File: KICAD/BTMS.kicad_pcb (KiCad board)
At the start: 2 copper layers, 0.1 x 46.8 mm, 139 parts, among them J1 Conn_01x05_Male, J2 AUX_Charge, J3 Battery_IO, J4 Power_Out, J5 BTemp, J6 DSKY, J7 key, J8 ICSP, P1 USB_C_Plug, Q1 SSM3K341R, Q2 DMN65D8L, Q3 SSM3K341R, Q4 FDN340P, Q5 FDN340P, Q6 FDN340P, Q7 DMN65D8L, Q8 DMN65D8L, U1 ACS711xLCTR-25AB, U10 BA033CC0FP-E2, U11 AON7522E, U12 AON7522E, U13 LM62CIM3/NOPB, U14 FAN3100TSX, U15 FAN3100TSX, U16 AON7522E, U17 dsPIC30F3011-PT, U18 FT230XQ, U2 AP33771, U3 IS281-4, U4 Q294700DSGR, U5 SCF4030-12-0X, U6 AONR21321, U7 ACS711xLCTR-25AB, U8 IS281-4, U9 IRS2184

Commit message: Fixed 3.3v regulator not having correct pinout. Progressed board layout.
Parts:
- added J9: Heater, Connector_PinHeader_2.54mm:PinHeader_1x02_P2.54mm_Vertical, F.Cu at (183.5, 143.4)
- J1: value Conn_01x05_Male -> Batt_Ballance
- J7: value key -> PWR_SW
- moved J7 189.1 mm to (205.0, 143.3), turned to -90 degrees
- moved C24 178.3 mm to (112.9, 132.3), turned to -90 degrees
- moved D18 173.8 mm to (115.0, 127.6), turned to 90 degrees
- moved C16 173.2 mm to (112.8, 136.0), turned to 90 degrees
- moved C32 172.8 mm to (115.3, 96.8)
- moved C35 168.2 mm to (118.9, 97.0)
- moved C20 166.2 mm to (115.4, 123.9)
- moved C12 165.5 mm to (120.4, 136.8), turned to 90 degrees
- moved Q4 161.4 mm to (190.3, 104.4), turned to 90 degrees
- moved U7 161.2 mm to (116.7, 134.6), turned to -90 degrees
- moved C41 160.7 mm to (189.0, 113.3), turned to -90 degrees
- moved L1 160.1 mm to (120.1, 110.2), turned to 90 degrees
- moved D24 159.4 mm to (187.2, 113.3), turned to 90 degrees
- moved R10 158.4 mm to (113.4, 119.6), turned to 90 degrees
- moved C42 157.0 mm to (190.0, 116.6), turned to -90 degrees
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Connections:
- Q3 pad 3: unconnected-(Q3-Pad3) -> Net-(Q3-Pad3)
- U10 pad 1: GND -> Net-(C13-Pad1)
- U10 pad 2: +5C -> GND
- U10 pad 3: Net-(C13-Pad1) -> +5C
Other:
- board size 0.1 x 46.8 mm -> 99.8 x 59.4 mm

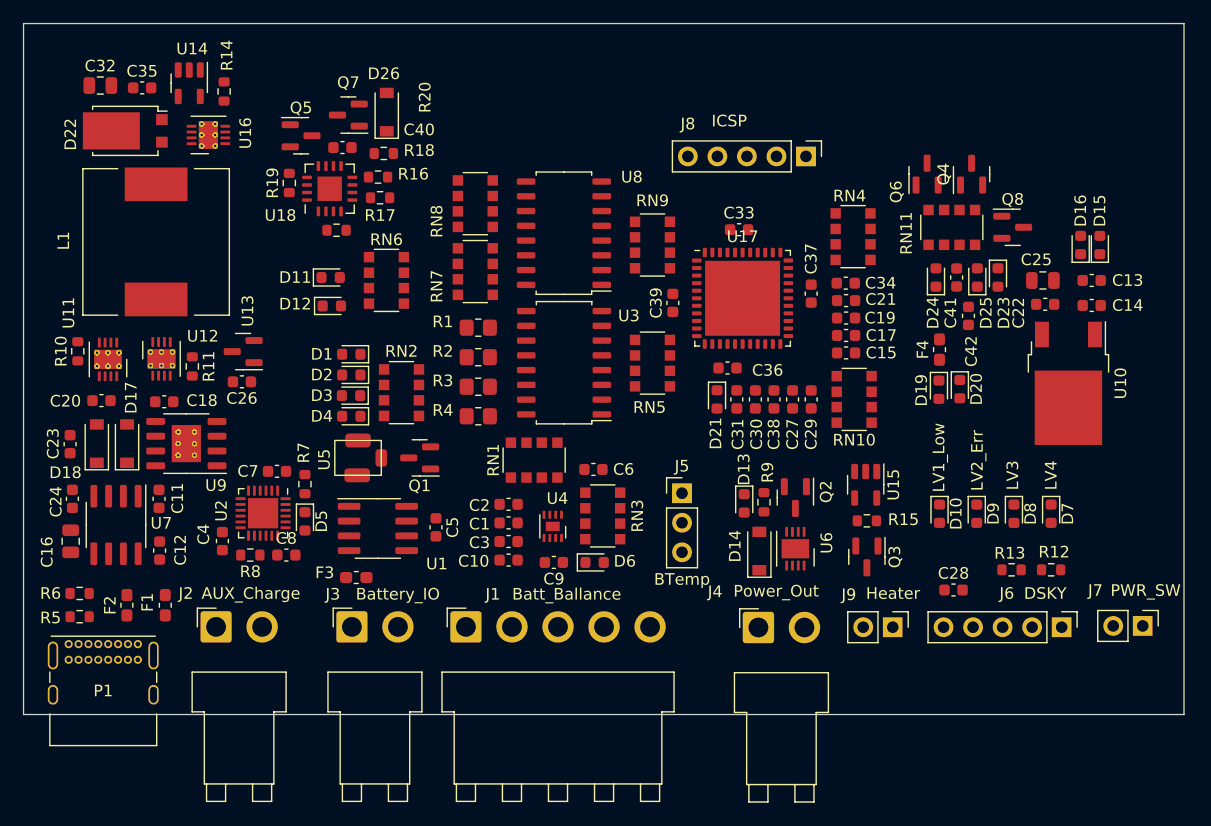
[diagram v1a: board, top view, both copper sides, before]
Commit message: Shrunk silkscreen text to compact parts more.
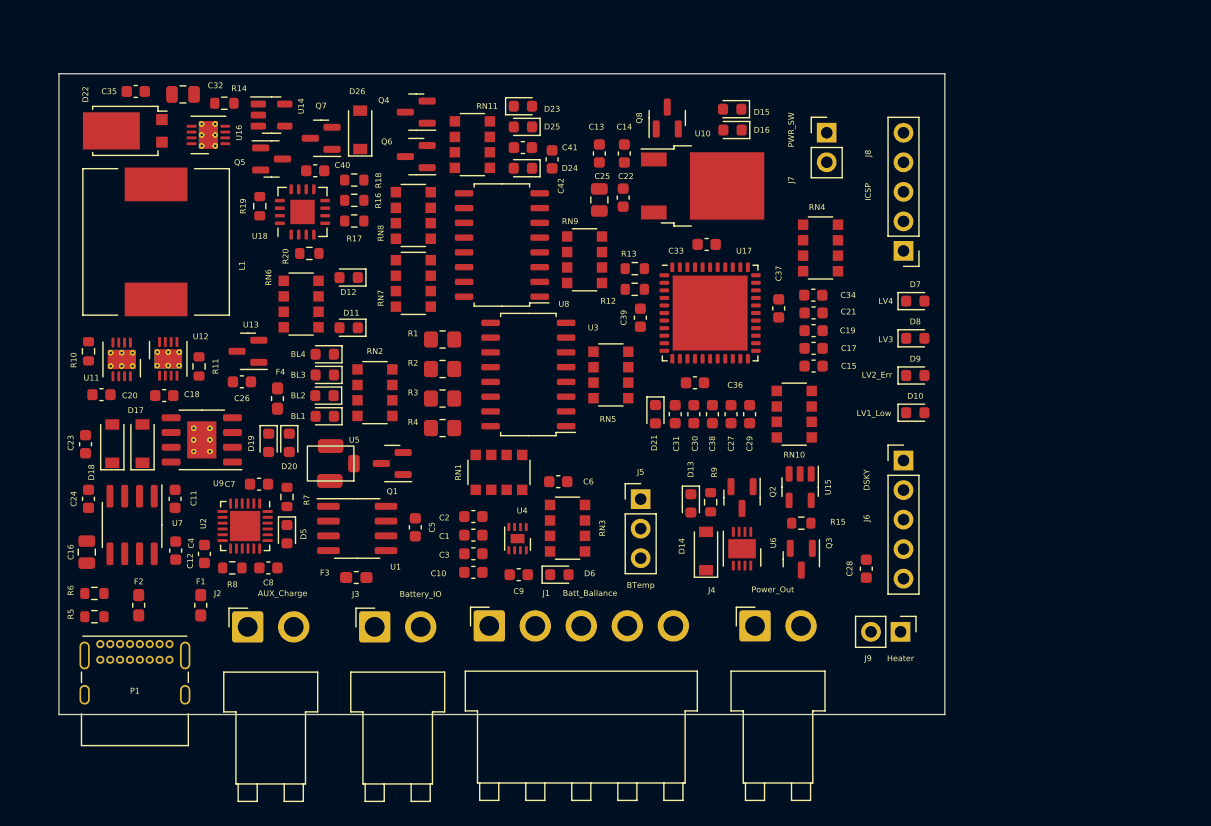
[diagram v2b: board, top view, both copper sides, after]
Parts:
- moved D20 57.9 mm to (131.6, 127.5)
- moved D19 57.8 mm to (129.8, 127.5)
- moved F4 57.1 mm to (130.6, 123.7), turned to -90 degrees
- moved J7 50.4 mm to (177.8, 100.8), turned to 0 degrees
- moved Q4 48.1 mm to (142.5, 99.1), turned to 180 degrees
- moved Q6 44.0 mm to (142.5, 102.9), turned to 180 degrees
- moved C13 43.7 mm to (158.2, 102.6), turned to -90 degrees
- moved D23 43.4 mm to (151.7, 98.6), turned to 0 degrees
- moved R12 43.2 mm to (161.3, 114.3), turned to 0 degrees
- moved C14 42.3 mm to (160.4, 102.6), turned to -90 degrees
- moved RN11 41.9 mm to (147.3, 101.9), turned to 180 degrees
- moved R13 41.5 mm to (161.3, 112.5)
- moved D25 41.2 mm to (151.7, 100.3), turned to 180 degrees
- moved C41 39.0 mm to (151.7, 102.1), turned to 0 degrees
- moved C25 38.8 mm to (158.2, 106.6), turned to 90 degrees
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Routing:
- added copper zone on In1.Cu, net GND
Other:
- board size 99.8 x 59.4 mm -> 76.2 x 55.1 mm
- copper layers 2 -> 4

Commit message: Started running traces.
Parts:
- removed RN6: 10K, Resistor_SMD:R_Array_Convex_4x1206
- added C43: 1uf 25v BF, Capacitor_SMD:C_0603_1608Metric, F.Cu at (180.6, 140.7)
- added C44: 1uf 25v BF, Capacitor_SMD:C_0603_1608Metric, F.Cu at (127.0, 97.5)
- added D27: Diode40V, Diode_SMD:D_0603_1608Metric, F.Cu at (169.7, 97.0)
- added F5: 5A, Fuse:Fuse_1206_3216Metric, F.Cu at (178.1, 137.2)
- added FB1: FerriteBead, Resistor_SMD:R_1206_3216Metric, F.Cu at (124.7, 133.3)
- added FB2: FerriteBead, Resistor_SMD:R_1206_3216Metric, F.Cu at (159.0, 98.3)
- added FB3: FerriteBead, Resistor_SMD:R_1206_3216Metric, F.Cu at (174.2, 139.2)
- added FB4: FerriteBead, Resistor_SMD:R_1206_3216Metric, F.Cu at (123.2, 97.3)
- added R21: 91K, Resistor_SMD:R_0603_1608Metric, F.Cu at (159.0, 118.9)
- added R22: 10K, Resistor_SMD:R_0603_1608Metric, F.Cu at (125.5, 138.9)
- added R23: 10K, Resistor_SMD:R_0603_1608Metric, F.Cu at (129.8, 128.3)
- added R24: 10K, Resistor_SMD:R_0603_1608Metric, F.Cu at (130.3, 112.0)
- F1, F2: footprint Fuse:Fuse_0603_1608Metric_Pad1.05x0.95mm_HandSolder -> Fuse:Fuse_1206_3216Metric
- F3: value Fuse9A -> 10A; footprint Fuse:Fuse_0603_1608Metric_Pad1.05x0.95mm_HandSolder -> Fuse:Fuse_1206_3216Metric
- J5: value BTemp -> BT_LM62
- R5, R6: value 5.1K -> 5K1
- R7: footprint Resistor_SMD:R_0603_1608Metric -> Resistor_SMD:R_1206_3216Metric
- moved R7 18.0 mm to (113.8, 135.9), turned to -90 degrees
- moved D11 11.6 mm to (132.1, 128.3), turned to 90 degrees
- moved R14 9.40 mm to (135.4, 98.6), turned to 180 degrees
- moved C4 6.39 mm to (130.3, 139.2), turned to 0 degrees
- moved R8 6.20 mm to (132.8, 137.7), turned to -90 degrees
- moved C16 5.91 mm to (113.3, 131.1), turned to -90 degrees
- moved D1 5.39 mm to (133.9, 114.6)
- moved D2 5.39 mm to (133.9, 116.3)
- moved D3 5.39 mm to (133.8, 118.1)
- moved D4 5.39 mm to (133.9, 119.9)
- moved F2 4.85 mm to (113.8, 141.0)
- moved C8 4.80 mm to (132.8, 134.6), turned to 90 degrees
- moved D5 4.71 mm to (128.3, 131.8), turned to 0 degrees
- moved R6 4.38 mm to (119.1, 141.2), turned to -90 degrees
- moved D20 4.13 mm to (132.3, 123.4)
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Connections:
- C11 pad 1: VBUS -> Net-(C11-Pad1)
- C32 pad 1: /ExtBus -> Net-(C32-Pad1)
- C35 pad 1: /ExtBus -> Net-(C32-Pad1)
- D15 pad 1: Net-(C13-Pad1) -> Net-(D15-Pad1)
- D16 pad 1: Net-(C13-Pad1) -> Net-(D15-Pad1)
- D22 pad 3: /ExtBus -> Net-(C32-Pad1)
- F2 pad 2: VBUS -> Net-(F2-Pad2)
- F3 pad 1: Net-(F3-Pad1) -> Net-(J3-Pad1)
- F3 pad 2: Net-(F3-Pad2) -> /BattIn
- J3 pad 1: Net-(F3-Pad2) -> Net-(J3-Pad1)
- J9 pad 1: /ExtBus -> Net-(J9-Pad1)
- J9 pad 2: Net-(Q3-Pad3) -> Net-(J9-Pad2)
- R7 pad 2: Net-(R7-Pad2) -> Net-(F2-Pad2)
- RN3 pad 8: /LBatt_Cell_4 -> /BattIn
- U1 pad 3: Net-(F3-Pad1) -> /BattIn
- U1 pad 4: Net-(F3-Pad1) -> /BattIn
- U2 pad 1: Net-(R7-Pad2) -> Net-(F2-Pad2)
- U2 pad 6: /GPIO4 -> Net-(U2-Pad6)
- U7 pad 1: VBUS -> Net-(C11-Pad1)
- U7 pad 2: VBUS -> Net-(C11-Pad1)
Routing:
- net +5C: track 0.00 -> 32.5 mm, vias 0 -> 3
- net /CC2: track 0.00 -> 31.0 mm, vias 0 -> 2
- net /BTStrapSig: track 0.00 -> 26.3 mm
- net /CC1: track 0.00 -> 21.9 mm, vias 0 -> 2
- net GND: track 0.00 -> 18.7 mm, vias 0 -> 32
- net Net-(F2-Pad2): track 0.00 -> 16.2 mm, vias 0 -> 2
- net Net-(D11-Pad2): track 0.00 -> 15.6 mm, vias 0 -> 2
- net Net-(R10-Pad1): track 0.00 -> 14.2 mm, vias 0 -> 2
- net Net-(C23-Pad1): track 0.00 -> 8.45 mm
- net Net-(R11-Pad1): track 0.00 -> 7.10 mm
- net /IntSwitched: track 0.00 -> 5.26 mm
- net VBUS: track 0.00 -> 3.99 mm, vias 0 -> 32
- net Net-(U2-Pad6): track 0.00 -> 2.17 mm
- net /HighCHfet: track 0.00 -> 2.07 mm
- net /LowCHfet: track 0.00 -> 1.84 mm
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- added copper zone on F.Cu, net /BTStrapSig
- added copper zone on F.Cu, net GND
- added copper zone on F.Cu, net Net-(C11-Pad1)
- added copper zone on B.Cu, net Net-(C16-Pad1)
- added copper zone on F.Cu, net Net-(C16-Pad1)
- added copper zone on F.Cu, net Net-(F2-Pad2)
- added copper zone on F.Cu, net Net-(J2-Pad1)
- added copper zone on B.Cu, net Net-(P1-PadA4)
- added copper zone on F.Cu, net Net-(P1-PadA4)
- added copper zone on In2.Cu, net Net-(P1-PadA4)
- added copper zone on B.Cu, net VBUS
- added copper zone on F.Cu, net VBUS
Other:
- board text added: "3v3"
- board text added: "5v-25v"
- board text added: "B+"
- board text added: "GND"
- board text added: "P-Out"
- board text added: "S-1"
- board text added: "S-2"
- board text added: "S-3"
- board text added: "S-4"
- board text added: "SIG"

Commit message: Continued routing.
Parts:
- moved C32 8.65 mm to (113.3, 100.1)
- moved R14 5.11 mm to (130.8, 100.8), turned to 0 degrees
- moved C44 3.84 mm to (130.8, 97.0), turned to 0 degrees
- moved U14 3.70 mm to (134.6, 98.3), turned to 180 degrees
- moved D22 2.06 mm to (118.5, 100.8)
- moved C36 0.55 mm to (166.1, 121.9)
- moved D12 0.54 mm to (133.6, 112.6)
- moved R20 0.54 mm to (137.2, 111.8)
- moved R24 0.54 mm to (130.3, 112.6)
- moved R16 0.54 mm to (137.2, 108.2)
- moved R17 0.54 mm to (137.2, 110.0)
- moved R19 0.54 mm to (129.0, 107.7)
- moved U18 0.54 mm to (132.7, 108.2)
- moved Q5 0.51 mm to (131.1, 103.6)
- moved C40 0.51 mm to (135.1, 104.6)
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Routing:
- net VBUS: track 3.99 -> 104.4 mm, vias 32 -> 34
- net GND: track 18.7 -> 108.7 mm, vias 32 -> 156
- net +5C: track 32.5 -> 120.5 mm, vias 3 -> 21
- net /Mult_SEL: track 0.00 -> 68.8 mm, vias 0 -> 3
- net /LBatt_Cell_4: track 0.00 -> 67.5 mm, vias 0 -> 5
- net /LBatt_Cell_3: track 0.00 -> 67.2 mm, vias 0 -> 6
- net /LBatt_Cell_2: track 0.00 -> 59.3 mm, vias 0 -> 6
- net /USB_D-: track 0.00 -> 57.7 mm, vias 0 -> 2
- net /USB_D+: track 0.00 -> 55.5 mm, vias 0 -> 2
- net /LBatt_Cell_1: track 0.00 -> 52.5 mm, vias 0 -> 6
- net Net-(D6-Pad1): track 0.00 -> 52.0 mm, vias 0 -> 2
- net Net-(D7-Pad1): track 0.00 -> 40.0 mm, vias 0 -> 2
- net Net-(D8-Pad1): track 0.00 -> 35.3 mm, vias 0 -> 2
- net Net-(D9-Pad1): track 0.00 -> 31.8 mm, vias 0 -> 2
- net Net-(D10-Pad1): track 0.00 -> 29.8 mm, vias 0 -> 2
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- added copper zone on F.Cu, net +5C
- added copper zone on In2.Cu, net +5C
- added copper zone on B.Cu, net /BattIn
- added copper zone on F.Cu, net /BattIn
- added copper zone on In2.Cu, net /BattIn
- added copper zone on B.Cu, net /ExtBus
- added copper zone on F.Cu, net /ExtBus
- added copper zone on In2.Cu, net /ExtBus
- added copper zone on B.Cu, net /IntBus
- added copper zone on F.Cu, net /IntBus
- added copper zone on In2.Cu, net /IntBus
- added copper zone on F.Cu, net Net-(C32-Pad1)
- added copper zone on F.Cu, net Net-(D22-Pad1)
- added copper zone on B.Cu, net Net-(J2-Pad1)
- added copper zone on In2.Cu, net Net-(J2-Pad1)
- added copper zone on B.Cu, net Net-(J3-Pad1)
- added copper zone on F.Cu, net Net-(J3-Pad1)
- added copper zone on In2.Cu, net Net-(J3-Pad1)
- added copper zone on F.Cu, net Net-(Q1-Pad3)
- added copper zone on In2.Cu, net Net-(Q1-Pad3)
- added copper zone on In2.Cu, net VBUS

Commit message: Continued routing board.
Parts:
- moved D19 63.3 mm to (191.8, 138.4)
- moved D20 63.3 mm to (193.8, 138.4)
- moved F4 63.3 mm to (195.8, 138.2)
- moved D2 3.59 mm to (133.3, 119.9)
- moved D1 3.59 mm to (133.3, 118.1)
- moved D3 3.59 mm to (133.3, 121.7)
- moved D4 3.59 mm to (133.3, 123.4)
- moved R4 0.51 mm to (144.8, 126.2)
- moved R1 0.25 mm to (144.8, 117.9)
- moved R3 0.25 mm to (144.8, 123.4)
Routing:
- net Net-(RN10-Pad4): track 0.00 -> 80.0 mm, vias 0 -> 5
- net /ChargeVoltage: track 6.00 -> 66.6 mm, vias 0 -> 2
- net /U1RX: track 0.00 -> 55.3 mm, vias 0 -> 3
- net /U1TX: track 0.00 -> 49.2 mm, vias 0 -> 3
- net /LithCell_V1: track 4.73 -> 51.8 mm, vias 0 -> 3
- net /LithCell_V2: track 4.37 -> 48.7 mm, vias 0 -> 3
- net /LithCell_V3: track 4.45 -> 46.3 mm, vias 0 -> 3
- net /LithCell_V4: track 4.98 -> 44.4 mm, vias 0 -> 3
- net /LBatt_Cell_2: track 59.3 -> 78.6 mm, vias 6 -> 7
- net /LBatt_Cell_1: track 52.5 -> 69.7 mm, vias 6 -> 7
- net /LBatt_Cell_3: track 67.2 -> 81.6 mm, vias 6 -> 7
- net /LBatt_Cell_4: track 67.5 -> 81.6 mm, vias 5 -> 6
- net Net-(RN7-Pad1): track 0.00 -> 13.1 mm
- net VBUS: track 104.4 -> 117.2 mm, vias 34 -> 35
- net /LithCell_V-en: track 0.00 -> 12.0 mm
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
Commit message: Continued routing board.
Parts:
- moved R13 25.2 mm to (180.6, 128.8), turned to 180 degrees
- moved R12 23.1 mm to (180.6, 127.0), turned to 180 degrees
- moved C33 0.92 mm to (168.1, 110.0)
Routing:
- net /C_Fault: track 0.00 -> 156.2 mm, vias 0 -> 8
- net /CCsense_in: track 0.00 -> 102.4 mm, vias 0 -> 3
- net Net-(RN4-Pad3): track 0.00 -> 94.0 mm, vias 0 -> 3
- net /CHctrl+: track 0.00 -> 85.1 mm, vias 0 -> 3
- net /V_Bus_Stat: track 4.24 -> 67.1 mm, vias 0 -> 4
- net /CH_Boost+: track 0.00 -> 47.4 mm, vias 0 -> 2
- net /IntSwitched: track 10.3 -> 56.2 mm, vias 0 -> 3
- net /Pctrl_OUT: track 9.32 -> 54.6 mm, vias 0 -> 2
- net /PGMC: track 0.00 -> 43.0 mm, vias 0 -> 2
- net /IntBus: track 9.63 -> 49.3 mm, vias 9 -> 11
- net /PGMD: track 0.00 -> 37.5 mm, vias 0 -> 2
- net /U2TX: track 2.22 -> 36.5 mm, vias 0 -> 3
- net /U2RX: track 1.76 -> 34.8 mm, vias 0 -> 3
- net /__PwrKey: track 2.41 -> 33.2 mm, vias 0 -> 3
- net /MCLR: track 8.33 -> 35.5 mm, vias 0 -> 2
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
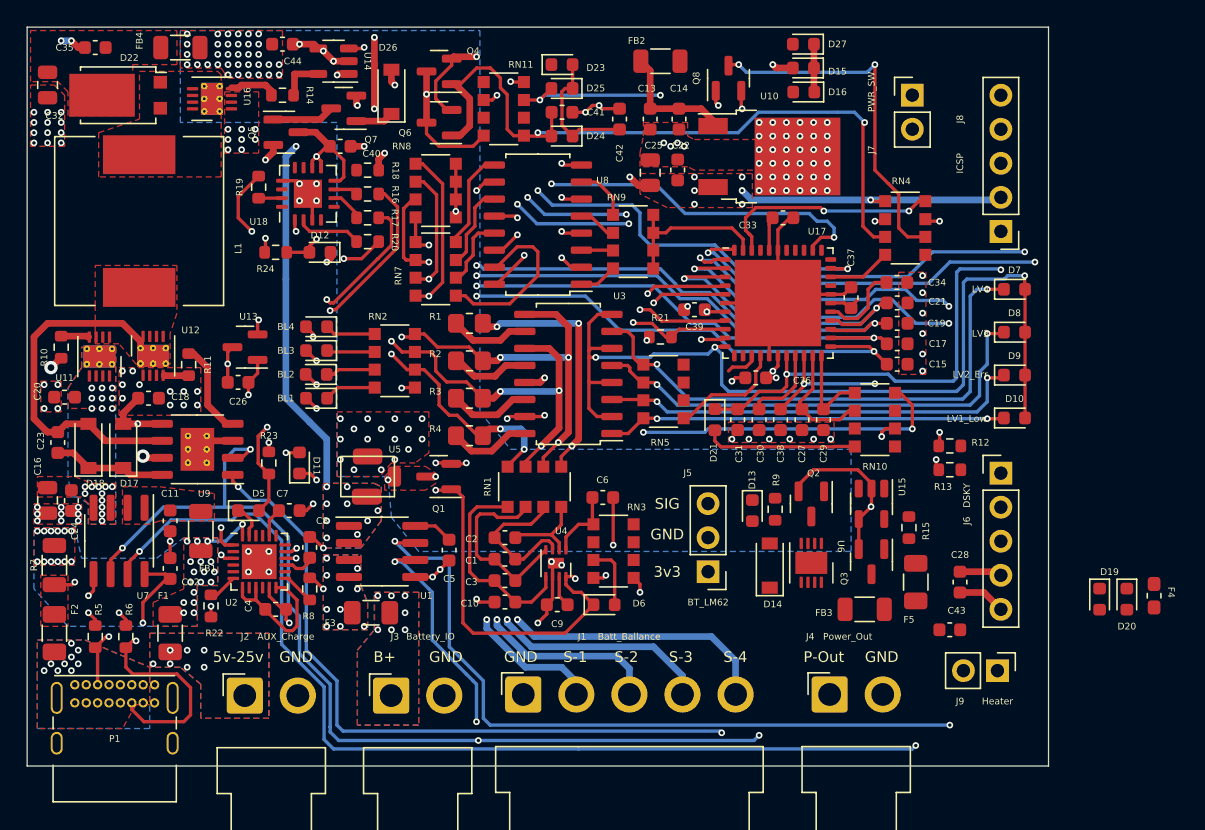
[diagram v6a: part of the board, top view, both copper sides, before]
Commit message: Board routing complete and cleaned up all board DRV violations except some silkscreen warning on the bottom edge.
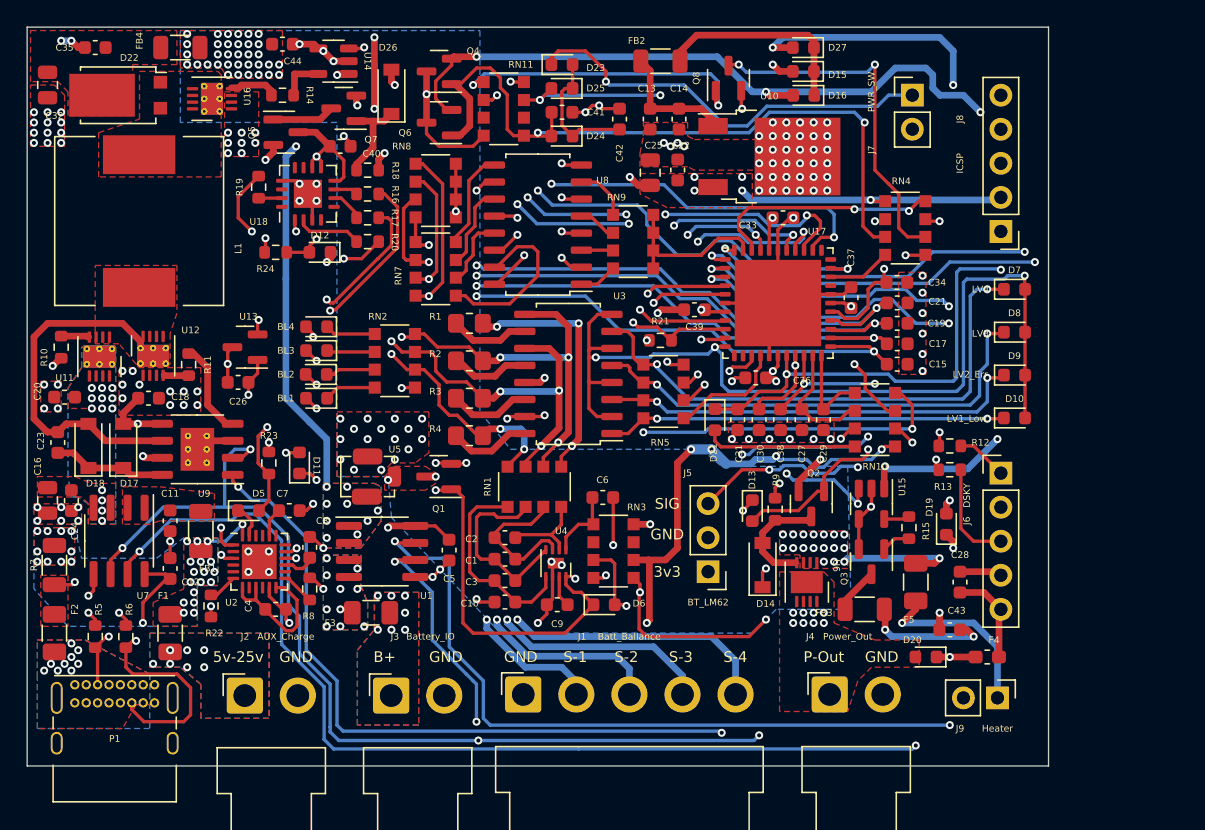
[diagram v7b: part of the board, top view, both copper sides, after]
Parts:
- moved D20 15.6 mm to (178.8, 142.7), turned to 180 degrees
- moved F4 13.3 mm to (183.4, 142.7), turned to 0 degrees
- moved D19 12.7 mm to (180.3, 132.8), turned to 90 degrees
- moved J9 2.03 mm to (184.2, 145.8)
- moved U6 1.47 mm to (169.9, 137.2)
- moved D14 0.54 mm to (166.6, 135.9)
- moved D15 0.25 mm to (169.7, 99.1)
- moved R21 0.25 mm to (159.0, 119.1)
- moved D16 0.25 mm to (169.7, 100.9)
- moved D27 0.25 mm to (169.7, 97.3)
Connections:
- U6 pad 6: unconnected-(U6-Pad6) -> /PowerOutput
- U6 pad 7: unconnected-(U6-Pad7) -> /PowerOutput
- U6 pad 8: unconnected-(U6-Pad8) -> /PowerOutput
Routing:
- net /IntSwitched: track 56.2 -> 135.8 mm, vias 3 -> 7
- net +5C: track 136.5 -> 213.2 mm, vias 17 -> 23
- net /PowerOutput: track 0.00 -> 62.9 mm, vias 0 -> 10
- net /BV_Fault: track 4.77 -> 53.7 mm, vias 0 -> 3
- net VBUS: track 117.2 -> 165.5 mm, vias 35 -> 34
- net /BattIn: track 0.00 -> 37.2 mm, vias 10 -> 11
- net /ChargeVoltage: track 66.6 -> 100.9 mm, vias 2 -> 4
- net Net-(D23-Pad1): track 0.00 -> 31.4 mm, vias 0 -> 1
- net /PO_EN: track 0.00 -> 28.8 mm, vias 0 -> 2
- net /Btemp_in: track 0.00 -> 25.7 mm, vias 0 -> 3
- net /Mult_B2: track 0.00 -> 24.2 mm, vias 0 -> 3
- net /Mult_B4: track 0.00 -> 22.5 mm, vias 0 -> 3
- net /KeepAlive: track 26.2 -> 47.7 mm, vias 2 -> 3
- net /Mult_B3: track 0.00 -> 19.4 mm, vias 0 -> 3
- net /Heat_CTRL: track 2.45 -> 21.5 mm, vias 0 -> 3
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- added copper zone on F.Cu, net /PowerOutput
- added copper zone on In2.Cu, net /PowerOutput
